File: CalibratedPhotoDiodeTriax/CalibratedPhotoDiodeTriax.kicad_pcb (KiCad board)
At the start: 2 copper layers, 50.8 x 50.8 mm, 2 parts, among them J1 TO-5 Photodiode Socket: Conn_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, J2 CBJ70 Triax Throughhole Conne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

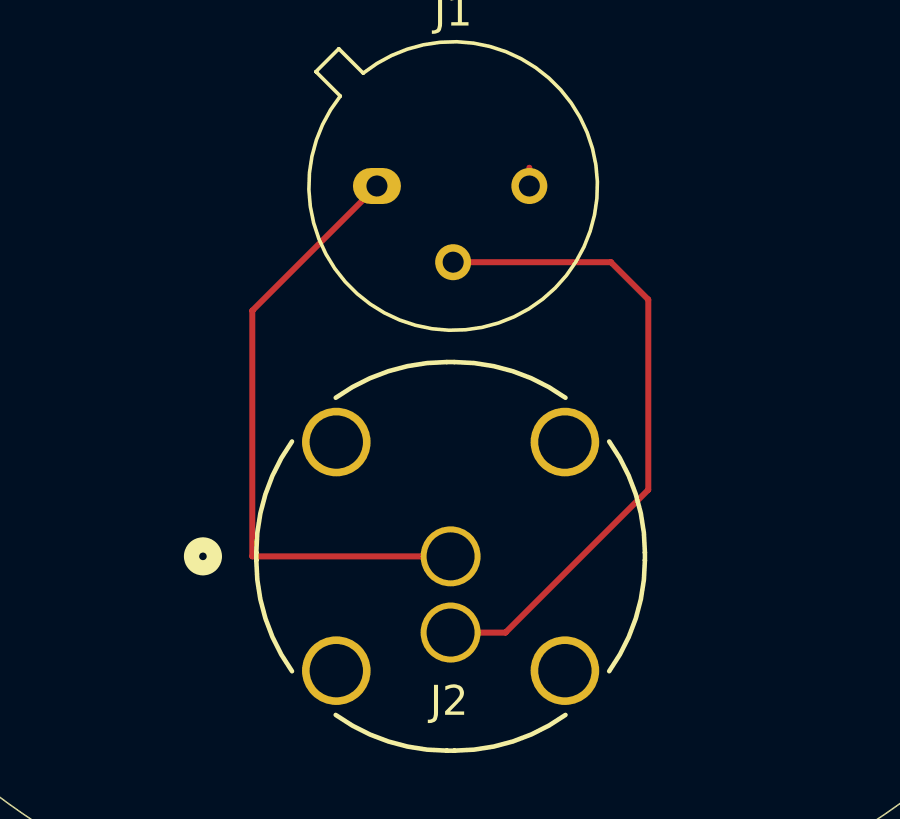
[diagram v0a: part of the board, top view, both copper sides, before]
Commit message: Swapped traces on triax connector
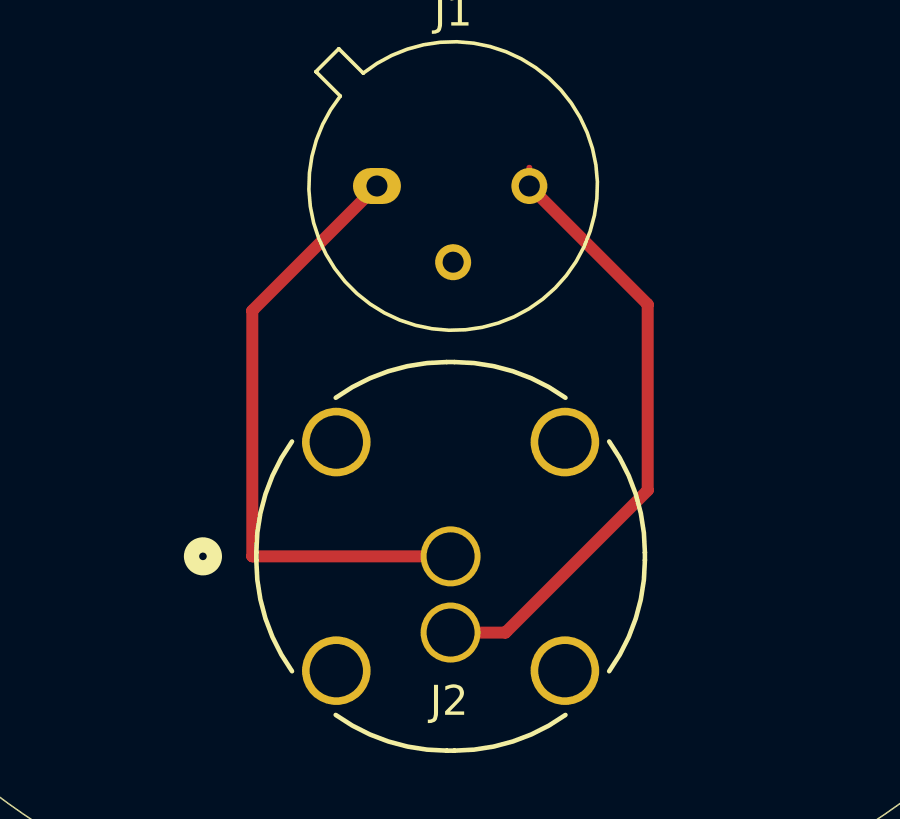
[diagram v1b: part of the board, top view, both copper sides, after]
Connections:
- J1 pad 2: Net-(J1-Pin_2) -> GND
- J1 pad 3: GND -> Net-(J1-Pin_3)
- J2 pad 2: Net-(J1-Pin_2) -> Net-(J1-Pin_3)
- J2 pad 4: GND -> (no net)
- J2 pad 5: GND -> (no net)
- J2 pad 6: GND -> (no net)
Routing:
- net Net-(J1-Pin_2): track 21.9 -> 0.00 mm
- net Net-(J1-Pin_3): track 0.00 -> 20.9 mm
- net GND: track 0.61 -> 0.00 mm
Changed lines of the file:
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@@
 	(net 0 "")
 	(net 1 "Net-(J1-Pin_1)")
-	(net 2 "Net-(J1-Pin_2)")
+	(net 2 "Net-(J1-Pin_3)")
 	(net 3 "GND")
 	(footprint "KiCADv6:CONN_CBJ70_CIN"
@@
 			(layers "*.Cu" "*.Mask")
 			(remove_unused_layers no)
-			(net 2 "Net-(J1-Pin_2)")
+			(net 2 "Net-(J1-Pin_3)")
 			(pinfunction "In2")
 			(pintype "passive")
@@
 			(layers "*.Cu" "*.Mask")
 			(remove_unused_layers no)
-			(net 3 "GND")
 		)
 		(pad "5" thru_hole circle
@@
 			(layers "*.Cu" "*.Mask")
 			(remove_unused_layers no)
-			(net 3 "GND")
 		)
 		(pad "6" thru_hole circle
@@
 			(layers "*.Cu" "*.Mask")
 			(remove_unused_layers no)
-			(net 3 "GND")
 		)
 		(embedded_fonts no)
@@
 			(layers "*.Cu" "*.Mask")
 			(remove_unused_layers no)
-			(net 2 "Net-(J1-Pin_2)")
+			(net 3 "GND")
 			(pinfunction "Pin_2")
 			(pintype "passive")
@@
 			(layers "*.Cu" "*.Mask")
 			(remove_unused_layers no)
-			(net 3 "GND")
+			(net 2 "Net-(J1-Pin_3)")
 			(pinfunction "Pin_3")
 			(pintype "passive")
@@
 		(start 153.08 72.9998)
 		(end 153.08 81.19)
-		(width 0.2)
+		(width 0.4)
 		(layer "F.Cu")
 		(net 1)
@@
 		(start 157.235 68.8448)
 		(end 153.08 72.9998)
-		(width 0.2)
+		(width 0.4)
 		(layer "F.Cu")
 		(net 1)
@@
 		(start 153.08 81.19)
 		(end 159.69 81.19)
-		(width 0.2)
+		(width 0.4)
 		(layer "F.Cu")
 		(net 1)
 	)
 	(segment
-		(start 159.775 71.3848)
-		(end 165.0348 71.3848)
-		(width 0.2)
+		(start 166.26 78.99)
+		(end 161.52 83.73)
+		(width 0.4)
 		(layer "F.Cu")
 		(net 2)
 	)
 	(segment
-		(start 161.52 83.73)
-		(end 159.69 83.73)
-		(width 0.2)
-		(layer "F.Cu")
-		(net 2)
-	)
-	(segment
-		(start 166.28 72.63)
-		(end 166.28 78.97)
-		(width 0.2)
-		(layer "F.Cu")
-		(net 2)
-	)
-	(segment
-		(start 166.28 78.97)
-		(end 161.52 83.73)
-		(width 0.2)
-		(layer "F.Cu")
-		(net 2)
-	)
-	(segment
-		(start 165.0348 71.3848)
-		(end 166.28 72.63)
-		(width 0.2)
+		(start 166.26 72.7898)
+		(end 166.26 78.99)
+		(width 0.4)
 		(layer "F.Cu")
 		(net 2)
@@
 		(width 0.2)
 		(layer "F.Cu")
-		(net 3)
+		(net 2)
+	)
+	(segment
+		(start 162.315 68.8448)
+		(end 166.26 72.7898)
+		(width 0.4)
+		(layer "F.Cu")
+		(net 2)
+	)
+	(segment
+		(start 161.52 83.73)
+		(end 159.69 83.73)
+		(width 0.4)
+		(layer "F.Cu")
+		(net 2)
 	)
 	(zone
